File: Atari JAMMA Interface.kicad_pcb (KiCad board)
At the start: 2 copper layers, 112.2 x 74.8 mm, 45 parts, among them P1 10K, U1 LM386, U2 DIP-14_W7.62mm, U3 MC34063AP, U4 74LS04

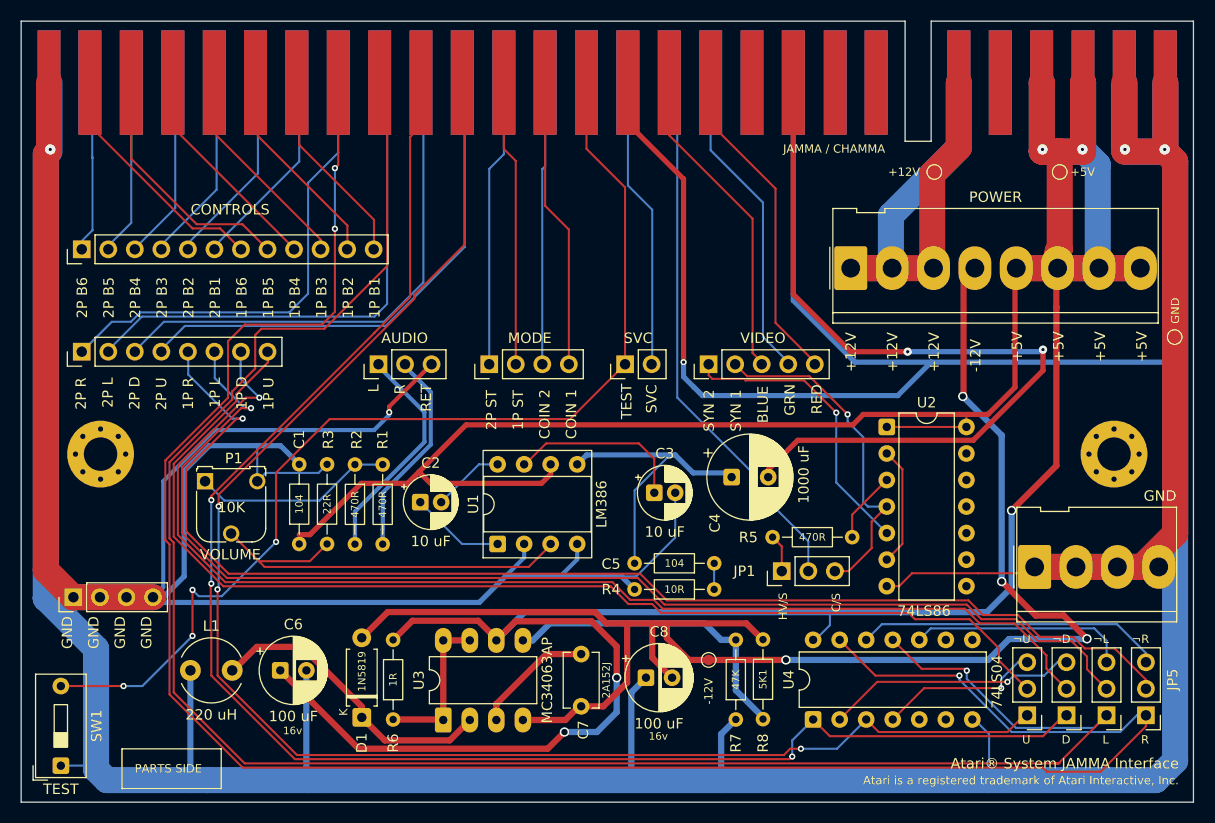
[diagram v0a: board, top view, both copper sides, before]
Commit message: add fifth ground contact to 3.96mm connector
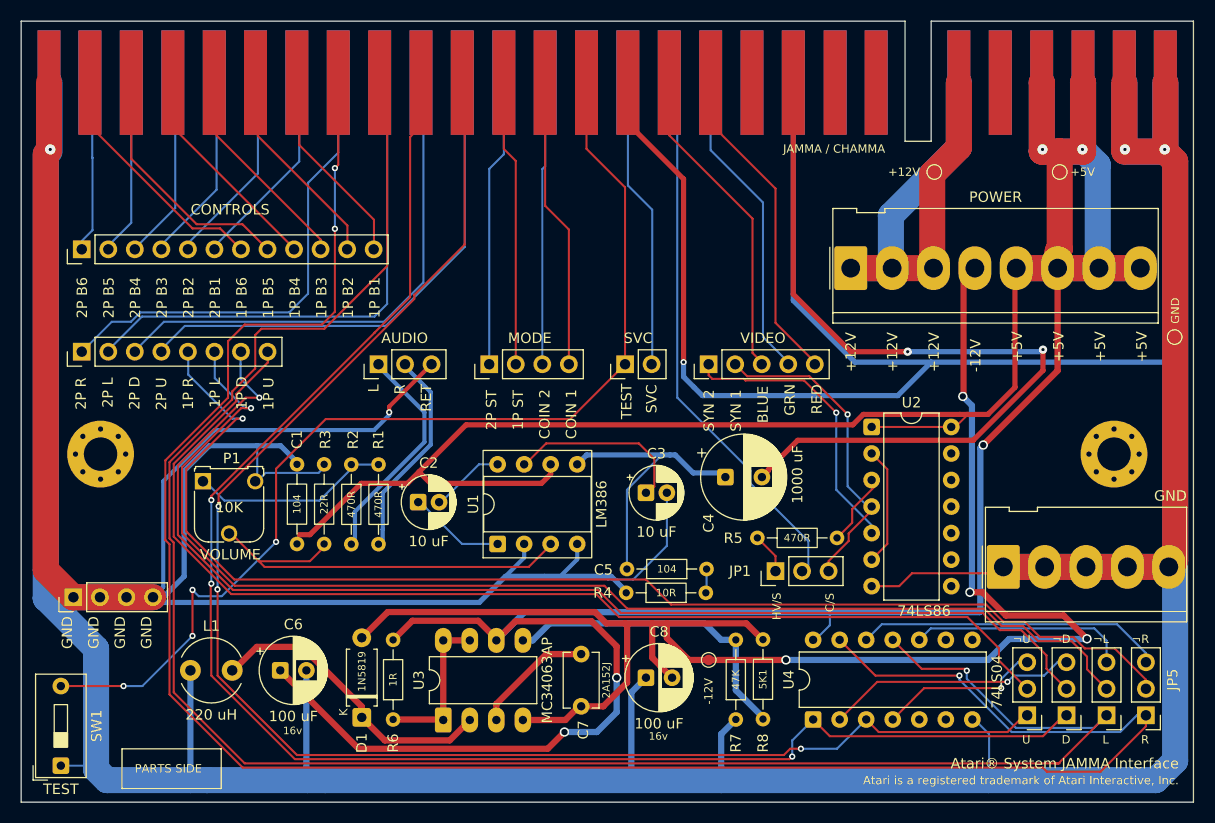
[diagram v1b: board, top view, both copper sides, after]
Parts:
- GND: value Molex_KK-396_5273-04A_1x04_P3.96mm_Vertical -> Molex_KK-396_5273-05A_1x05_P3.96mm_Vertical; footprint Connector_Molex:Molex_KK-396_5273-04A_1x04_P3.96mm_Vertical -> Connector_Molex:Molex_KK-396_5273-05A_1x05_P3.96mm_Vertical
- moved GND 3.00 mm to (187.4, 115.6)
- moved R5 1.46 mm to (163.9, 112.8)
- moved U2 1.45 mm to (174.8, 102.2)
- moved C5 0.92 mm to (159.0, 115.8)
- moved R4 0.86 mm to (158.9, 118.1)
- moved C3 0.80 mm to (153.2, 108.5)
- moved C4 0.60 mm to (160.8, 107.0)
- moved HV/S 0.60 mm to (165.6, 116.0)
- moved R1 0.40 mm to (127.6, 105.8)
- moved R2 0.35 mm to (125.0, 105.8)
- moved R3 0.28 mm to (122.4, 113.4)
- moved C1 0.21 mm to (119.8, 113.4)
- moved P1 0.20 mm to (110.8, 107.4)
- moved C2 0.20 mm to (131.4, 109.4)
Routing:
- net GND: track 723.4 -> 731.3 mm
- net VID_SYN1: track 33.2 -> 30.6 mm
- net -12V: track 149.5 -> 152.0 mm
- net PREAMP_OUT: track 27.8 -> 28.5 mm
- net VID_NXOR_R5: track 6.84 -> 7.36 mm

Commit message: add video ground, replace 2.54mm grounds with 3.96
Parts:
- removed Ground: PinHeader_1x04_P2.54mm_Vertical, Connector_PinHeader_2.54mm:PinHeader_1x04_P2.54mm_Vertical
- added GND: Molex_KK-396_5273-03A_1x03_P3.96mm_Vertical, Connector_Molex:Molex_KK-396_5273-03A_1x03_P3.96mm_Vertical, F.Cu at (95.8, 115.6)
- VIDEO: value PinHeader_1x05_P2.54mm_Vertical -> PinHeader_1x06_P2.54mm_Vertical; footprint Connector_PinHeader_2.54mm:PinHeader_1x05_P2.54mm_Vertical -> Connector_PinHeader_2.54mm:PinHeader_1x06_P2.54mm_Vertical
- moved AUDIO 2.20 mm to (125.4, 96.2)
- moved MODE 2.20 mm to (136.0, 96.2)
- moved SVC 2.20 mm to (149.0, 96.2)
- moved VIDEO 2.20 mm to (157.0, 96.2)
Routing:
- net VID_CSYNC: track 52.5 -> 55.4 mm
- net VID_SYN1: track 30.6 -> 32.8 mm
- net TEST: track 102.4 -> 100.6 mm
- net VID_SYN2: track 28.1 -> 29.7 mm
- net 1P_U: track 149.7 -> 151.0 mm
- net AUDIO_R: track 20.3 -> 19.1 mm
- net AUDIO_L: track 21.9 -> 20.7 mm
- net VID_G: track 30.3 -> 29.1 mm
- net VID_R: track 31.4 -> 30.2 mm
- net VID_B: track 30.9 -> 29.7 mm
- net COIN_2: track 27.1 -> 28.0 mm
- net SERVICE: track 27.9 -> 27.0 mm
- net COIN_1: track 27.9 -> 27.0 mm
- net 2P_START: track 27.5 -> 28.4 mm
- net 1P_D: track 154.3 -> 155.2 mm
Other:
- board text added: "B"
- board text added: "G"
- board text removed: "BLUE"
- board text removed: "GRN"
- board text removed: "RED"

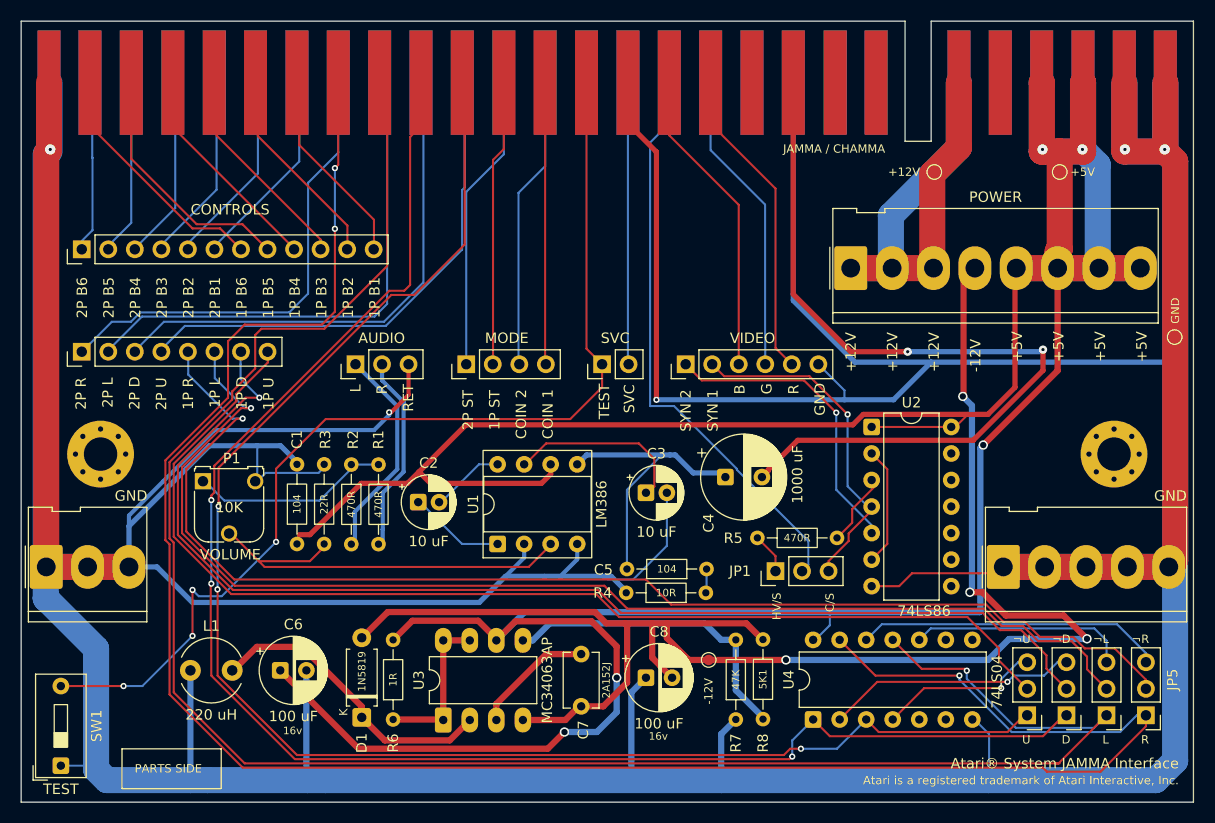
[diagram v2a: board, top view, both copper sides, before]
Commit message: even out grounds
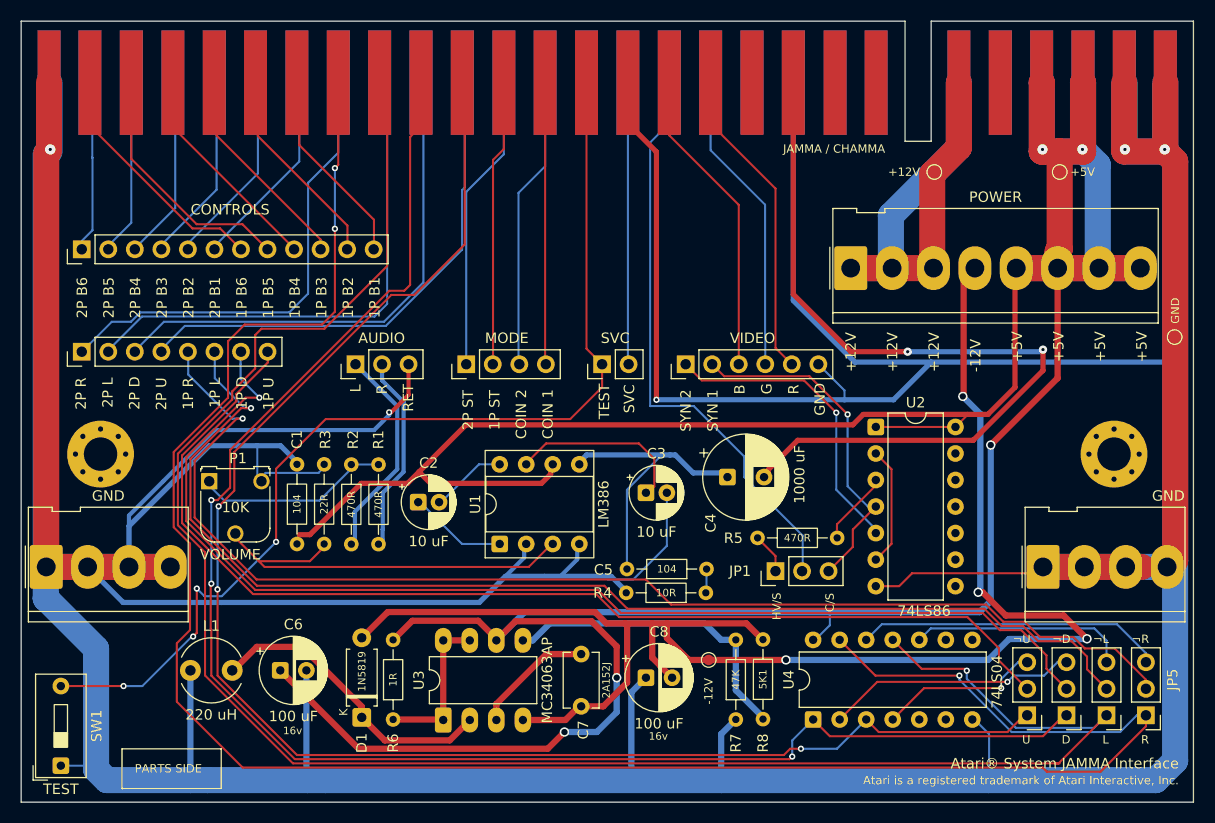
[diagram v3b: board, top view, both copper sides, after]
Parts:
- GND: value Molex_KK-396_5273-03A_1x03_P3.96mm_Vertical -> Molex_KK-396_5273-04A_1x04_P3.96mm_Vertical; footprint Connector_Molex:Molex_KK-396_5273-03A_1x03_P3.96mm_Vertical -> Connector_Molex:Molex_KK-396_5273-04A_1x04_P3.96mm_Vertical
- GND: value Molex_KK-396_5273-05A_1x05_P3.96mm_Vertical -> Molex_KK-396_5273-04A_1x04_P3.96mm_Vertical; footprint Connector_Molex:Molex_KK-396_5273-05A_1x05_P3.96mm_Vertical -> Connector_Molex:Molex_KK-396_5273-04A_1x04_P3.96mm_Vertical
- moved GND 3.80 mm to (191.2, 115.6)
- moved P1 0.60 mm to (111.4, 107.4)
- moved U2 0.40 mm to (175.2, 102.2)
- moved C4 0.20 mm to (161.0, 107.0)
- moved U1 0.20 mm to (139.2, 113.4)
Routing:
- net GND: track 731.4 -> 735.2 mm
- net 1P_L: track 190.2 -> 186.8 mm
- net 1P_R_OUT: track 121.1 -> 119.2 mm
- net 1P_L_OUT: track 117.8 -> 115.9 mm
- net 1P_D_OUT: track 114.2 -> 112.3 mm
- net 1P_U_OUT: track 109.8 -> 108.0 mm
- net VID_CSYNC: track 55.4 -> 56.0 mm
- net VID_SYN1: track 32.8 -> 33.4 mm
